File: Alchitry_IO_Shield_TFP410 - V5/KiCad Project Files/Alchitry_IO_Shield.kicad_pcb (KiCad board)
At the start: 2 copper layers, 65 x 45 mm, 58 parts, among them J1 HDMI_A_1.4, Q1 Q_PMOS_SGD, Q2 Q_PMOS_SGD, Q3 Q_PMOS_SGD, Q4 Q_PMOS_SGD, SW1 SWL3, SW2 SWL1, SW3 SWL2, SW4 SWL4, SW5 SWR3, SW6 SWR1, SW7 SWR2, SW8 SWR3, U1 Alchitry_Single, U2 TFP410, U3 0402_7Seg_CA, U4 0402_7Seg_CA, U5 0402_7Seg_CA, U6 0402_7Seg_CA

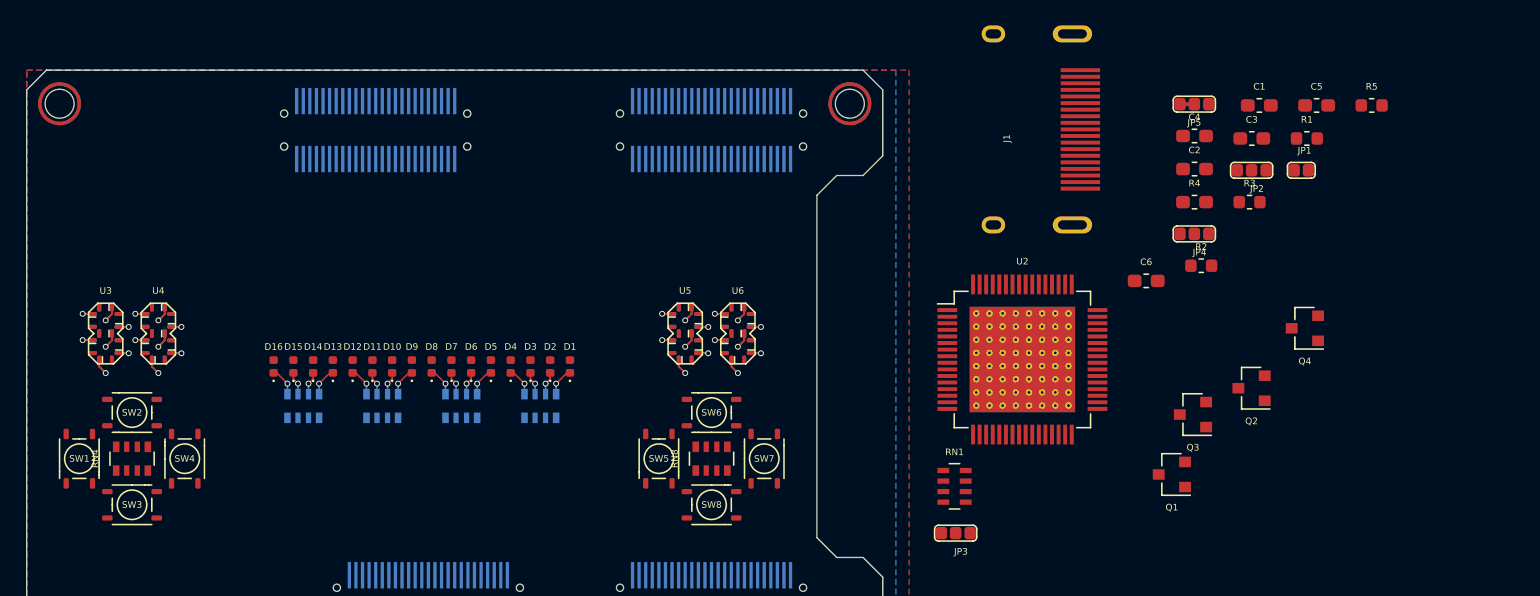
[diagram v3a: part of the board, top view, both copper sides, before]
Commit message: replaced 7segs with custom footprints
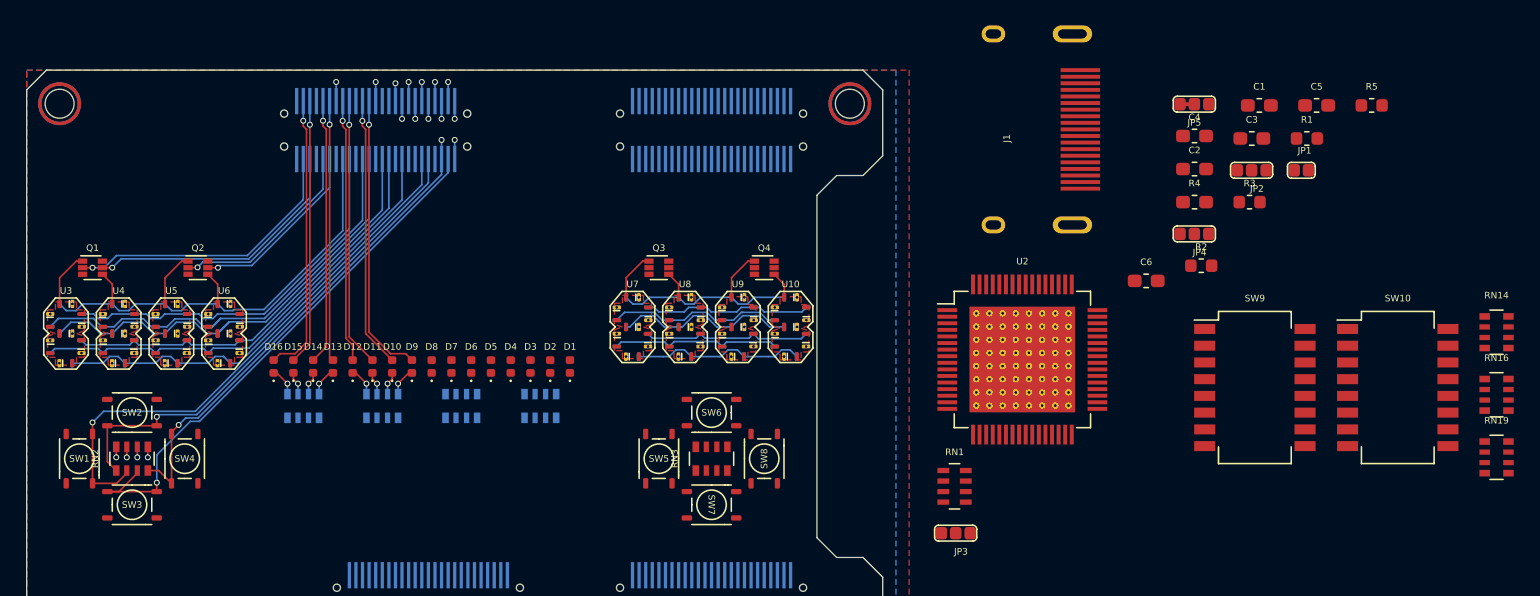
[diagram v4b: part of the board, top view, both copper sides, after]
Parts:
- removed RN4, RN8: R_Pack04, Resistor_SMD:R_Array_Convex_4x0603
- added RN14: R_Pack04, Resistor_SMD:R_Array_Convex_4x0603, F.Cu at (123.6, 31.9)
- added RN16: R_Pack04, Resistor_SMD:R_Array_Convex_4x0603, F.Cu at (123.6, 36.6)
- added RN19: R_Pack04, Resistor_SMD:R_Array_Convex_4x0603, F.Cu at (123.6, 41.4)
- added RN2: R_Pack04, Resistor_SMD:R_Array_Convex_4x0603, F.Cu at (20.0, 41.5)
- added RN3: R_Pack04, Resistor_SMD:R_Array_Convex_4x0603, F.Cu at (64.0, 41.5)
- added SW10: SW_DIP_x08, Button_Switch_SMD:SW_DIP_SPSTx08_Slide_Copal_CHS-08B_W7.62mm_P1.27mm, F.Cu at (116.1, 36.1)
- added SW9: SW_DIP_x08, Button_Switch_SMD:SW_DIP_SPSTx08_Slide_Copal_CHS-08B_W7.62mm_P1.27mm, F.Cu at (105.2, 36.1)
- added U10: 0402_7Seg_CA, Custom_LEDs:0402_7Seg_CA_W_Res, F.Cu at (70.0, 31.5)
- added U7: 0402_7Seg_CA, Custom_LEDs:0402_7Seg_CA_W_Res, F.Cu at (58.0, 31.5)
- added U8: 0402_7Seg_CA, Custom_LEDs:0402_7Seg_CA_W_Res, F.Cu at (62.0, 31.5)
- added U9: 0402_7Seg_CA, Custom_LEDs:0402_7Seg_CA_W_Res, F.Cu at (66.0, 31.5)
- Q1, Q2, Q3, Q4: value Q_PMOS_SGD -> NTZD3152P; footprint Package_TO_SOT_SMD:SOT-23 -> Package_TO_SOT_SMD:SOT-563
- SW1: value SWL3 -> SW3
- SW2: value SWL1 -> SW1
- SW3: value SWL2 -> SW2
- SW4: value SWL4 -> SW4
- SW5: value SWR3 -> SW3
- SW6: value SWR1 -> SW1
- SW7: value SWR2 -> SW2
- SW8: value SWR3 -> SW4
- moved Q1 83.4 mm to (17.0, 27.0), turned to 0 degrees
- moved Q2 80.5 mm to (25.0, 27.0), turned to 0 degrees
- moved Q3 42.1 mm to (60.0, 27.0), turned to 0 degrees
- moved Q4 41.3 mm to (68.0, 27.0), turned to 0 degrees
- moved U5 39.0 mm to (23.0, 32.0)
- moved U6 39.0 mm to (27.0, 32.0)
- moved SW7 5.32 mm to (64.0, 45.0), turned to 180 degrees
- moved SW8 5.32 mm to (68.0, 41.5), turned to -90 degrees
- moved U3 3.02 mm to (15.0, 32.0)
- moved U4 3.02 mm to (19.0, 32.0)
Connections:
- Q1 pad 1: /AN0 -> Net-(Q1-Pad1)
- Q1 pad 2: Net-(Q1-Pad2) -> /ANL1
- Q2 pad 1: +3V3 -> Net-(Q2-Pad1)
- Q2 pad 2: Net-(Q2-Pad2) -> /ANL3
- Q3 pad 1: /AN2 -> Net-(Q3-Pad1)
- Q3 pad 2: Net-(Q3-Pad2) -> (no net)
- Q4 pad 1: /AN3 -> Net-(Q4-Pad1)
- Q4 pad 2: Net-(Q4-Pad2) -> (no net)
- U1 pad A_11: (no net) -> /CL5
- U1 pad A_12: (no net) -> /CL7
- U1 pad A_14: (no net) -> /CL2
- U1 pad A_15: (no net) -> /CL4
- U1 pad A_17: (no net) -> /CL3
- U1 pad A_2: /C6 -> /ANL1
- U1 pad A_20: (no net) -> /SWL3
- U1 pad A_21: (no net) -> /SWL1
- U1 pad A_23: /LED15 -> /SWL4
- U1 pad A_24: /LED14 -> /SWL2
- U1 pad A_27: (no net) -> /DIP14
- U1 pad A_28: (no net) -> /DIP15
- U1 pad A_3: /C5 -> /ANL2
- U1 pad A_39: (no net) -> /LED8
- U1 pad A_40: (no net) -> /LED9
- U1 pad A_42: (no net) -> /LED10
- U1 pad A_43: /AN0 -> /LED11
- U1 pad A_45: /C4 -> /LED12
- U1 pad A_46: /C3 -> /LED13
- U1 pad A_48: /C2 -> /LED14
- U1 pad A_49: (no net) -> /LED15
- U1 pad A_5: /C0 -> /ANL3
- U1 pad A_6: /C1 -> /ANL4
- U1 pad A_8: /AN2 -> /CL6
- U1 pad A_9: /AN3 -> /CL1
- U1 pad B_2: /LED13 -> (no net)
- U1 pad B_3: /LED12 -> (no net)
- U1 pad B_30: (no net) -> /DIP0
- U1 pad B_31: (no net) -> /DIP1
- U1 pad B_33: (no net) -> /DIP2
- U1 pad B_34: (no net) -> /DIP3
- U1 pad B_36: (no net) -> /DIP4
- U1 pad B_37: (no net) -> /DIP5
- U1 pad B_39: (no net) -> /DIP6
- U1 pad B_40: (no net) -> /DIP7
- U1 pad B_42: (no net) -> /DIP8
- U1 pad B_43: (no net) -> /DIP9
- U1 pad B_45: (no net) -> /DIP10
- U1 pad B_46: (no net) -> /DIP11
- U1 pad B_48: (no net) -> /DIP12
- U1 pad B_49: (no net) -> /DIP13
- U1 pad B_5: /LED11 -> (no net)
- U1 pad B_6: /LED10 -> (no net)
- U1 pad B_8: /LED9 -> (no net)
- U1 pad B_9: /LED8 -> (no net)
- U3 pad 1: /C0 -> /CL1
- U3 pad 10: Net-(U3-Pad10) -> (no net)
- U3 pad 11: Net-(U3-Pad11) -> (no net)
- U3 pad 12: Net-(U3-Pad12) -> (no net)
- U3 pad 13: Net-(U3-Pad13) -> (no net)
- U3 pad 14: Net-(U3-Pad14) -> (no net)
- U3 pad 15: Net-(U3-Pad15) -> (no net)
- U3 pad 2: /C1 -> /CL2
- U3 pad 3: /C2 -> /CL3
- U3 pad 4: /C3 -> /CL4
- U3 pad 5: /C4 -> /CL5
- U3 pad 6: /C5 -> /CL6
- U3 pad 7: /C6 -> /CL7
- U3 pad 8: Net-(Q1-Pad2) -> Net-(Q1-Pad1)
- U3 pad 9: Net-(U3-Pad9) -> (no net)
- U4 pad 1: /C0 -> /CL1
- U4 pad 10: Net-(U4-Pad10) -> (no net)
- U4 pad 11: Net-(U4-Pad11) -> (no net)
- U4 pad 12: Net-(U4-Pad12) -> (no net)
- U4 pad 13: Net-(U4-Pad13) -> (no net)
- U4 pad 14: Net-(U4-Pad14) -> (no net)
- U4 pad 15: Net-(U4-Pad15) -> (no net)
- U4 pad 2: /C1 -> /CL2
- U4 pad 3: /C2 -> /CL3
- U4 pad 4: /C3 -> /CL4
- U4 pad 5: /C4 -> /CL5
- U4 pad 6: /C5 -> /CL6
- U4 pad 7: /C6 -> /CL7
- U4 pad 8: Net-(Q2-Pad2) -> Net-(Q1-Pad4)
- U4 pad 9: Net-(U4-Pad9) -> (no net)
- U5 pad 1: /C0 -> /CL1
- U5 pad 10: Net-(U5-Pad10) -> (no net)
- U5 pad 11: Net-(U5-Pad11) -> (no net)
- U5 pad 12: Net-(U5-Pad12) -> (no net)
- U5 pad 13: Net-(U5-Pad13) -> (no net)
- U5 pad 14: Net-(U5-Pad14) -> (no net)
- U5 pad 15: Net-(U5-Pad15) -> (no net)
- U5 pad 2: /C1 -> /CL2
- U5 pad 3: /C2 -> /CL3
- U5 pad 4: /C3 -> /CL4
- U5 pad 5: /C4 -> /CL5
- U5 pad 6: /C5 -> /CL6
- U5 pad 7: /C6 -> /CL7
- U5 pad 8: Net-(Q3-Pad2) -> Net-(Q2-Pad1)
- U5 pad 9: Net-(U5-Pad9) -> (no net)
- U6 pad 1: /C0 -> /CL1
- U6 pad 10: Net-(U6-Pad10) -> (no net)
- U6 pad 11: Net-(U6-Pad11) -> (no net)
- U6 pad 12: Net-(U6-Pad12) -> (no net)
- U6 pad 13: Net-(U6-Pad13) -> (no net)
- U6 pad 14: Net-(U6-Pad14) -> (no net)
- U6 pad 15: Net-(U6-Pad15) -> (no net)
- U6 pad 2: /C1 -> /CL2
- U6 pad 3: /C2 -> /CL3
- U6 pad 4: /C3 -> /CL4
- U6 pad 5: /C4 -> /CL5
- U6 pad 6: /C5 -> /CL6
- U6 pad 7: /C6 -> /CL7
- U6 pad 8: Net-(Q4-Pad2) -> Net-(Q2-Pad4)
- U6 pad 9: Net-(U6-Pad9) -> (no net)
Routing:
- net /SWL3: track 0.00 -> 42.2 mm, vias 0 -> 1
- net /SWL2: track 0.00 -> 41.6 mm, vias 0 -> 1
- net /SWL1: track 0.00 -> 37.9 mm, vias 0 -> 1
- net /SWL4: track 0.00 -> 37.3 mm, vias 0 -> 2
- net /CL7: track 0.00 -> 35.2 mm
- net /CL4: track 0.00 -> 34.9 mm
- net /CL3: track 0.00 -> 34.5 mm
- net /CL5: track 0.00 -> 34.1 mm
- net /CL2: track 0.00 -> 31.7 mm
- net /CL6: track 0.00 -> 30.9 mm
- net /CL1: track 0.00 -> 29.1 mm
- net /ANL1: track 0.00 -> 22.0 mm, vias 0 -> 1
- net /LED8: track 0.00 -> 21.7 mm, vias 0 -> 1
- net /LED15: track 0.00 -> 21.5 mm, vias 0 -> 1
- net /ANL2: track 0.00 -> 20.9 mm, vias 0 -> 1
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- added copper zone on F.Cu, net Net-(Q1-Pad1)
- added copper zone on F.Cu, net Net-(Q1-Pad4)
- added copper zone on F.Cu, net Net-(Q2-Pad1)
- added copper zone on F.Cu, net Net-(Q2-Pad4)
- added copper zone on F.Cu, net Net-(Q3-Pad1)
- added copper zone on F.Cu, net Net-(Q3-Pad4)
- added copper zone on F.Cu, net Net-(Q4-Pad1)
- added copper zone on F.Cu, net Net-(Q4-Pad4)

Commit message: laid out switches, btns and leds
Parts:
- removed C1, C2, C3, C4, C5, C6: 100nF, Capacitor_SMD:C_0603_1608Metric_Pad1.05x0.95mm_HandSolder
- removed J1: HDMI_A_1.4, Custom_Parts:HDMI
- removed JP1: DKEN, Custom_Parts:Jumper_2_Pin_Unbridged
- removed JP2: DK2, Custom_Parts:jumper_unbridged
- removed JP3: DK1, Custom_Parts:jumper_unbridged
- removed JP4: DK3, Custom_Parts:jumper_unbridged
- removed JP5: V_Sel, Custom_Parts:jumper_1_2_bridged
- removed R1: 33K, Resistor_SMD:R_0603_1608Metric
- removed R2: 91K, Resistor_SMD:R_0603_1608Metric
- removed R3, R5: 10K, Resistor_SMD:R_0603_1608Metric
- removed R4: 510, Resistor_SMD:R_0603_1608Metric_Pad1.05x0.95mm_HandSolder
- removed RN1: 10K, Resistor_SMD:R_Array_Concave_4x0603
- removed U2: TFP410, Package_QFP:HTQFP-64-1EP_10x10mm_P0.5mm_EP8x8mm_Mask4.4x4.4mm_ThermalVias
- added G***: LOGO, LOGO, F.Cu at (42.0, 36.5)
- added RN4: R_Pack04, Resistor_SMD:R_Array_Convex_4x0603, B.Cu at (38.0, 44.0)
- RN14, RN16, RN19: moved to B.Cu
- moved RN14 91.4 mm to (33.0, 44.0), turned to -90 degrees
- moved RN19 77.6 mm to (46.0, 44.0), turned to -90 degrees
- moved RN16 73.0 mm to (51.0, 44.0), turned to -90 degrees
- moved SW9 70.2 mm to (35.5, 44.0), turned to 90 degrees
- moved SW10 68.1 mm to (48.5, 44.0), turned to 90 degrees
- moved D1 2.50 mm to (53.2, 32.0)
- moved D10 2.50 mm to (39.8, 32.0)
- moved D11 2.50 mm to (38.2, 32.0)
- moved D12 2.50 mm to (36.8, 32.0)
- moved D13 2.50 mm to (35.2, 32.0)
- moved D14 2.50 mm to (33.8, 32.0)
- moved D15 2.50 mm to (32.2, 32.0)
- moved D16 2.50 mm to (30.8, 32.0)
- moved D2 2.50 mm to (51.8, 32.0)
- moved D3 2.50 mm to (50.2, 32.0)
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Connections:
- D1 pad 2: /LED0 -> /LED1
- D10 pad 2: /LED9 -> /LED10
- D11 pad 2: /LED10 -> /LED11
- D12 pad 2: /LED11 -> /LED12
- D13 pad 2: /LED12 -> /LED13
- D14 pad 2: /LED13 -> /LED14
- D15 pad 2: /LED14 -> /LED15
- D16 pad 2: /LED15 -> /LED16
- D2 pad 2: /LED1 -> /LED2
- D3 pad 2: /LED2 -> /LED3
- D4 pad 2: /LED3 -> /LED4
- D5 pad 2: /LED4 -> /LED5
- D6 pad 2: /LED5 -> /LED6
- D7 pad 2: /LED6 -> /LED7
- D8 pad 2: /LED7 -> /LED8
- D9 pad 2: /LED8 -> /LED9
- Q3 pad 2: (no net) -> /ANR1
- Q3 pad 5: (no net) -> /ANR2
- Q4 pad 2: (no net) -> /ANR3
- Q4 pad 5: (no net) -> /ANR4
- RN14 pad 5: /DIP7 -> /DIP13
- RN14 pad 6: /DIP6 -> /DIP14
- RN14 pad 7: /DIP5 -> /DIP15
- RN14 pad 8: /DIP4 -> /DIP16
- RN16 pad 5: /DIP11 -> /DIP1
- RN16 pad 6: /DIP10 -> /DIP2
- RN16 pad 7: /DIP9 -> /DIP3
- RN16 pad 8: /DIP8 -> /DIP4
- RN19 pad 5: /DIP15 -> /DIP5
- RN19 pad 6: /DIP14 -> /DIP6
- RN19 pad 7: /DIP13 -> /DIP7
- RN19 pad 8: /DIP12 -> /DIP8
- SW10 pad 1: /DIP15 -> /DIP8
- SW10 pad 2: /DIP14 -> /DIP7
- SW10 pad 3: /DIP13 -> /DIP6
- SW10 pad 4: /DIP12 -> /DIP5
- SW10 pad 5: /DIP11 -> /DIP4
- SW10 pad 6: /DIP10 -> /DIP3
- SW10 pad 7: /DIP9 -> /DIP2
- SW10 pad 8: /DIP8 -> /DIP1
- SW9 pad 1: /DIP7 -> /DIP16
- SW9 pad 2: /DIP6 -> /DIP15
- SW9 pad 3: /DIP5 -> /DIP14
- SW9 pad 4: /DIP4 -> /DIP13
- SW9 pad 5: /DIP3 -> /DIP12
- SW9 pad 6: /DIP2 -> /DIP11
- SW9 pad 7: /DIP1 -> /DIP10
- SW9 pad 8: /DIP0 -> /DIP9
- U1 pad A_27: /DIP14 -> /LED1
- U1 pad A_28: /DIP15 -> /LED2
- U1 pad A_30: (no net) -> /LED3
- U1 pad A_31: (no net) -> /LED4
- U1 pad A_33: (no net) -> /LED5
- U1 pad A_34: (no net) -> /LED6
- U1 pad A_36: (no net) -> /LED7
- U1 pad A_37: (no net) -> /LED8
- U1 pad A_39: /LED8 -> /LED9
- U1 pad A_40: /LED9 -> /LED10
- U1 pad A_42: /LED10 -> /LED11
- U1 pad A_43: /LED11 -> /LED12
- U1 pad A_45: /LED12 -> /LED13
- U1 pad A_46: /LED13 -> /LED14
- U1 pad A_48: /LED14 -> /LED15
- U1 pad A_49: /LED15 -> /LED16
- U1 pad B_11: /LED7 -> /CR2
- U1 pad B_12: /LED6 -> /CR7
- U1 pad B_14: /LED5 -> /CR5
- U1 pad B_15: /LED4 -> /CR1
- U1 pad B_17: /LED3 -> /CR6
- U1 pad B_18: /LED2 -> (no net)
- U1 pad B_2: (no net) -> /SWR2
- U1 pad B_20: /LED1 -> /ANR1
- U1 pad B_21: /LED0 -> /ANR2
- U1 pad B_23: /SWL3 -> /ANR3
- U1 pad B_24: /SWL4 -> /ANR4
- U1 pad B_27: /SWL2 -> (no net)
- U1 pad B_28: /SWL1 -> (no net)
- U1 pad B_3: (no net) -> /SWR3
- U1 pad B_30: /DIP0 -> (no net)
- U1 pad B_31: /DIP1 -> (no net)
- U1 pad B_33: /DIP2 -> (no net)
- U1 pad B_34: /DIP3 -> (no net)
- U1 pad B_36: /DIP4 -> (no net)
- U1 pad B_37: /DIP5 -> (no net)
- U1 pad B_39: /DIP6 -> (no net)
- U1 pad B_40: /DIP7 -> (no net)
- U1 pad B_42: /DIP8 -> (no net)
- U1 pad B_43: /DIP9 -> (no net)
- U1 pad B_45: /DIP10 -> (no net)
- U1 pad B_46: /DIP11 -> (no net)
- U1 pad B_48: /DIP12 -> (no net)
- U1 pad B_49: /DIP13 -> (no net)
- U1 pad B_5: (no net) -> /SWR1
- U1 pad B_6: (no net) -> /SWR4
- U1 pad B_8: (no net) -> /CR3
- U1 pad B_9: (no net) -> /CR4
- U1 pad C_20: /B0 -> (no net)
- U1 pad C_21: /B1 -> (no net)
- U1 pad C_23: /B2 -> (no net)
- U1 pad C_24: /B3 -> (no net)
- U1 pad C_27: /G3 -> /DIP1
- U1 pad C_28: /G2 -> /DIP2
- U1 pad C_30: /G1 -> /DIP3
- U1 pad C_31: /G0 -> /DIP4
- U1 pad C_33: /R3 -> /DIP5
- U1 pad C_34: /R2 -> /DIP6
- U1 pad C_36: /R1 -> /DIP7
- U1 pad C_37: /R0 -> /DIP8
- U1 pad C_39: /HS -> /DIP9
- U1 pad C_40: /VS -> /DIP10
- U1 pad C_42: /DE -> /DIP11
- U1 pad C_43: /CLK -> /DIP12
- U1 pad C_45: /SWR4 -> /DIP13
- U1 pad C_46: /SWR1 -> /DIP14
- U1 pad C_48: /SWR3 -> /DIP15
- U1 pad C_49: /SWR2 -> /DIP16
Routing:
- net /SWR2: track 0.00 -> 42.5 mm, vias 0 -> 1
- net /SWR1: track 0.00 -> 41.6 mm, vias 0 -> 1
- net /SWR4: track 0.00 -> 38.9 mm, vias 0 -> 1
- net /SWR3: track 0.00 -> 33.8 mm, vias 0 -> 1
- net /LED1: track 0.00 -> 23.2 mm, vias 0 -> 2
- net /LED5: track 0.00 -> 22.0 mm, vias 0 -> 2
- net /LED4: track 0.00 -> 21.3 mm, vias 0 -> 2
- net /LED3: track 0.00 -> 21.2 mm, vias 0 -> 1
- net /LED2: track 0.00 -> 20.6 mm, vias 0 -> 1
- net /CR3: track 13.3 -> 33.6 mm
- net /CR2: track 12.9 -> 33.1 mm
- net /LED7: track 0.00 -> 20.0 mm, vias 0 -> 1
- net /LED6: track 0.00 -> 19.3 mm, vias 0 -> 1
- net /LED16: track 0.00 -> 19.0 mm, vias 0 -> 1
- net /CR4: track 12.9 -> 30.9 mm
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
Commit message: adding USB C for OTG programming and serial
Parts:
- added J2: C168714_HDMI_Atype, Custom_Connectors:C168714_HDMI_Atype, F.Cu at (63.0, 20.4)
- added JP6: V_Sel, Custom_Parts:jumper_unbridged, B.Cu at (63.0, 17.4)
- moved D1 15.9 mm to (53.2, 47.9)
- moved D10 15.9 mm to (39.8, 47.9)
- moved D11 15.9 mm to (38.2, 47.9)
- moved D12 15.9 mm to (36.8, 47.9)
- moved D13 15.9 mm to (35.2, 47.9)
- moved D14 15.9 mm to (33.8, 47.9)
- moved D15 15.9 mm to (32.2, 47.9)
- moved D16 15.9 mm to (30.8, 47.9)
- moved D2 15.9 mm to (51.8, 47.9)
- moved D3 15.9 mm to (50.2, 47.9)
- moved D4 15.9 mm to (48.8, 47.9)
- moved D5 15.9 mm to (47.2, 47.9)
- moved D6 15.9 mm to (45.8, 47.9)
- moved D7 15.9 mm to (44.2, 47.9)
- moved D8 15.9 mm to (42.8, 47.9)
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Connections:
- U1 pad B_39: (no net) -> /CK-
- U1 pad B_40: (no net) -> /CK+
- U1 pad B_42: (no net) -> /D0-
- U1 pad B_43: (no net) -> /D0+
- U1 pad B_45: (no net) -> /D1-
- U1 pad B_46: (no net) -> /D1+
- U1 pad B_48: (no net) -> /D2-
- U1 pad B_49: (no net) -> /D2+
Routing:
- net +3V3: track 2.90 -> 46.6 mm, vias 2 -> 32
- net +5V: track 0.00 -> 19.6 mm
- net /D2-: track 0.00 -> 10.3 mm, vias 0 -> 1
- net /D1-: track 0.00 -> 10.3 mm, vias 0 -> 1
- net /D0-: track 0.00 -> 10.3 mm, vias 0 -> 1
- net /CK-: track 0.00 -> 10.3 mm, vias 0 -> 1
- net /D2+: track 0.00 -> 10.2 mm, vias 0 -> 1
- net /D1+: track 0.00 -> 10.2 mm, vias 0 -> 1
- net /D0+: track 0.00 -> 10.2 mm, vias 0 -> 1
- net /CK+: track 0.00 -> 10.2 mm, vias 0 -> 1
- net Net-(J2-Pad18): track 0.00 -> 6.00 mm, vias 0 -> 1
- net GNDREF: track 9.10 -> 6.40 mm, vias 10 -> 8
- net /LED5: track 22.0 -> 20.6 mm, vias 2 -> 1
- net /LED4: track 21.3 -> 20.0 mm, vias 2 -> 1
- net /LED1: track 23.2 -> 21.9 mm, vias 2 -> 1
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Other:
- board size 65 x 45 mm -> 65 x 61.4 mm

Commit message: updated shield v4 schematic
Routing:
- net +5V: track 19.6 -> 36.6 mm, vias 0 -> 2
- net +3V3: track 46.6 -> 58.8 mm, vias 32 -> 33
- net Net-(J2-Pad18): track 6.00 -> 8.14 mm
- net GNDREF: track 6.40 -> 8.29 mm, vias 8 -> 9
- added copper zone on F.Cu, net GNDREF
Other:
- outline, holes or cut-outs redrawn
